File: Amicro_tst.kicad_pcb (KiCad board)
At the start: 2 copper layers, 16 parts, among them J1 Conn_01x04_Female, J2 Conn_01x05_Female, J3 Conn_01x04_Female, SW1 SW_Push, U1 ATmega328-P, U2 24LC512, Y1 Crystal

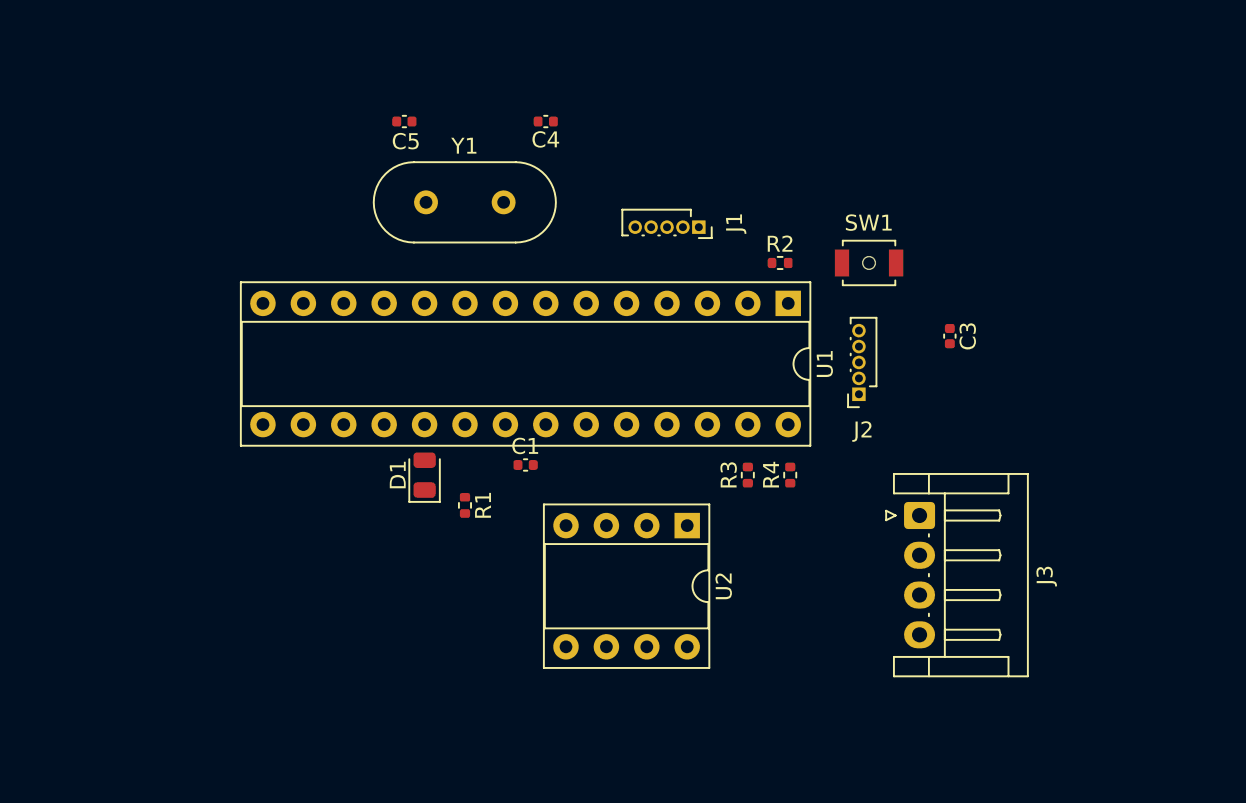
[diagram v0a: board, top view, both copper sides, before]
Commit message: redid lost work/testpoints
Redid lost work that didnt save, still need to find footprints for transistors
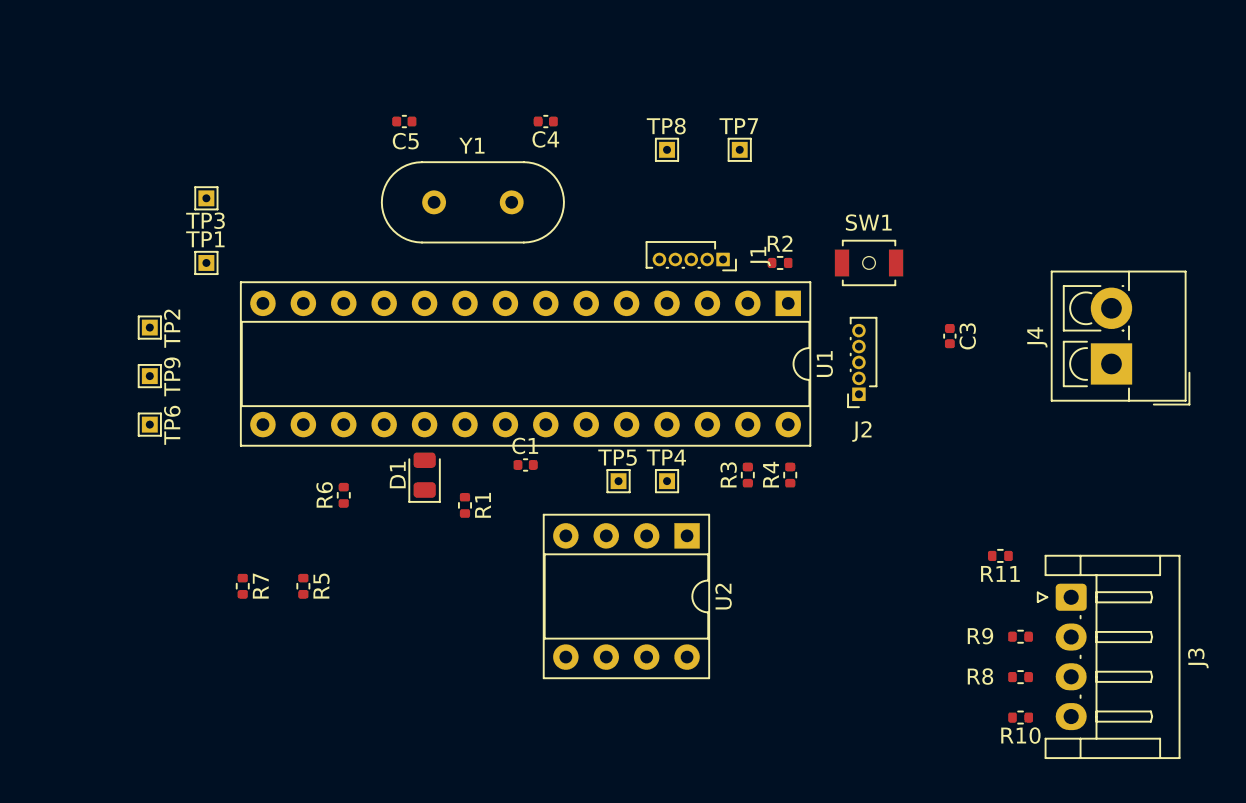
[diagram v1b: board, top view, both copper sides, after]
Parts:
- added J4: Screw_Terminal_01x02, TerminalBlock_4Ucon:TerminalBlock_4Ucon_1x02_P3.50mm_Vertical, F.Cu at (166.0, 124.1)
- added R10: 33, Resistor_SMD:R_0402_1005Metric, F.Cu at (160.3, 146.4)
- added R11: 33, Resistor_SMD:R_0402_1005Metric, F.Cu at (159.1, 136.2)
- added R5: 1k, Resistor_SMD:R_0402_1005Metric, F.Cu at (115.2, 138.1)
- added R6: 1k, Resistor_SMD:R_0402_1005Metric, F.Cu at (117.8, 132.4)
- added R7: 1k, Resistor_SMD:R_0402_1005Metric, F.Cu at (111.4, 138.1)
- added R8: 33, Resistor_SMD:R_0402_1005Metric, F.Cu at (160.3, 143.8)
- added R9: 33, Resistor_SMD:R_0402_1005Metric, F.Cu at (160.3, 141.3)
- added TP1: TstPin, TestPoint:TestPoint_THTPad_1.0x1.0mm_Drill0.5mm, F.Cu at (109.1, 117.8)
- added TP2: TstPin, TestPoint:TestPoint_THTPad_1.0x1.0mm_Drill0.5mm, F.Cu at (105.6, 121.8)
- added TP3: TstPin, TestPoint:TestPoint_THTPad_1.0x1.0mm_Drill0.5mm, F.Cu at (109.1, 113.7)
- added TP4: TstPin, TestPoint:TestPoint_THTPad_1.0x1.0mm_Drill0.5mm, F.Cu at (138.1, 131.5)
- added TP5: TstPin, TestPoint:TestPoint_THTPad_1.0x1.0mm_Drill0.5mm, F.Cu at (135.1, 131.5)
- added TP6: TstPin, TestPoint:TestPoint_THTPad_1.0x1.0mm_Drill0.5mm, F.Cu at (105.6, 127.9)
- added TP7: TstPin, TestPoint:TestPoint_THTPad_1.0x1.0mm_Drill0.5mm, F.Cu at (142.7, 110.7)
- added TP8: TstPin, TestPoint:TestPoint_THTPad_1.0x1.0mm_Drill0.5mm, F.Cu at (138.1, 110.7)
- added TP9: TstPin, TestPoint:TestPoint_THTPad_1.0x1.0mm_Drill0.5mm, F.Cu at (105.6, 124.9)
- moved J3 10.8 mm to (163.5, 138.8)
- moved J1 2.54 mm to (141.6, 117.6)
- moved U2 0.65 mm to (139.4, 134.9)
- moved Y1 0.51 mm to (123.5, 114.0)
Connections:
- J3 pad 1: unconnected-(J3-Pad1) -> Net-(J3-Pad1)
- J3 pad 2: unconnected-(J3-Pad2) -> Net-(J3-Pad2)
- J3 pad 3: unconnected-(J3-Pad3) -> Net-(J3-Pad3)
- J3 pad 4: unconnected-(J3-Pad4) -> Net-(J3-Pad4)
- U1 pad 12: unconnected-(U1-Pad12) -> Net-(U1-Pad12)
- U1 pad 13: unconnected-(U1-Pad13) -> Net-(U1-Pad13)
- U1 pad 14: unconnected-(U1-Pad14) -> Net-(U1-Pad14)
- U1 pad 15: unconnected-(U1-Pad15) -> PWM0
- U1 pad 16: unconnected-(U1-Pad16) -> PWM1
- U1 pad 17: unconnected-(U1-Pad17) -> PWM2
- U1 pad 24: unconnected-(U1-Pad24) -> Net-(U1-Pad24)
- U1 pad 25: unconnected-(U1-Pad25) -> Net-(U1-Pad25)
- U1 pad 26: unconnected-(U1-Pad26) -> Net-(U1-Pad26)
- U1 pad 4: unconnected-(U1-Pad4) -> Net-(U1-Pad4)
- U1 pad 5: unconnected-(U1-Pad5) -> Net-(U1-Pad5)
- U1 pad 6: unconnected-(U1-Pad6) -> Net-(U1-Pad6)

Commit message: transistor footprints
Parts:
- added Q1: Q_NPN_BEC, TO_SOT_Packages_SMD:SC-59_Handsoldering, F.Cu at (124.4, 136.6)
- added Q2: Q_NPN_BEC, TO_SOT_Packages_SMD:SC-59_Handsoldering, F.Cu at (119.3, 136.1)
- added Q3: Q_NPN_BEC, TO_SOT_Packages_SMD:SC-59_Handsoldering, F.Cu at (114.7, 136.1)
- J1: footprint Connector_PinSocket_1.00mm:PinSocket_1x05_P1.00mm_Vertical -> Connector_JST:JST_EH_S4B-EH_1x04_P2.50mm_Horizontal
- moved J3 56.9 mm to (107.1, 145.9), turned to 90 degrees
- moved R10 50.7 mm to (110.3, 138.4), turned to 0 degrees
- moved R8 50.1 mm to (110.3, 140.9), turned to 180 degrees
- moved R9 50.1 mm to (110.3, 143.4), turned to 0 degrees
- moved R11 45.2 mm to (115.7, 149.3), turned to 0 degrees
- moved R3 18.8 mm to (132.0, 146.2), turned to -90 degrees
- moved R4 18.3 mm to (135.6, 146.2), turned to -90 degrees
- moved TP3 9.16 mm to (118.3, 114.2)
- moved J1 8.79 mm to (148.6, 112.2), turned to 0 degrees
- moved R7 7.62 mm to (111.7, 130.5)
- moved R5 7.62 mm to (115.2, 130.5)
- moved TP1 7.06 mm to (115.2, 114.2)
- moved TP5 3.05 mm to (138.1, 131.5)
- moved TP4 2.54 mm to (135.6, 131.5)
- moved R6 2.16 mm to (118.8, 130.5)
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
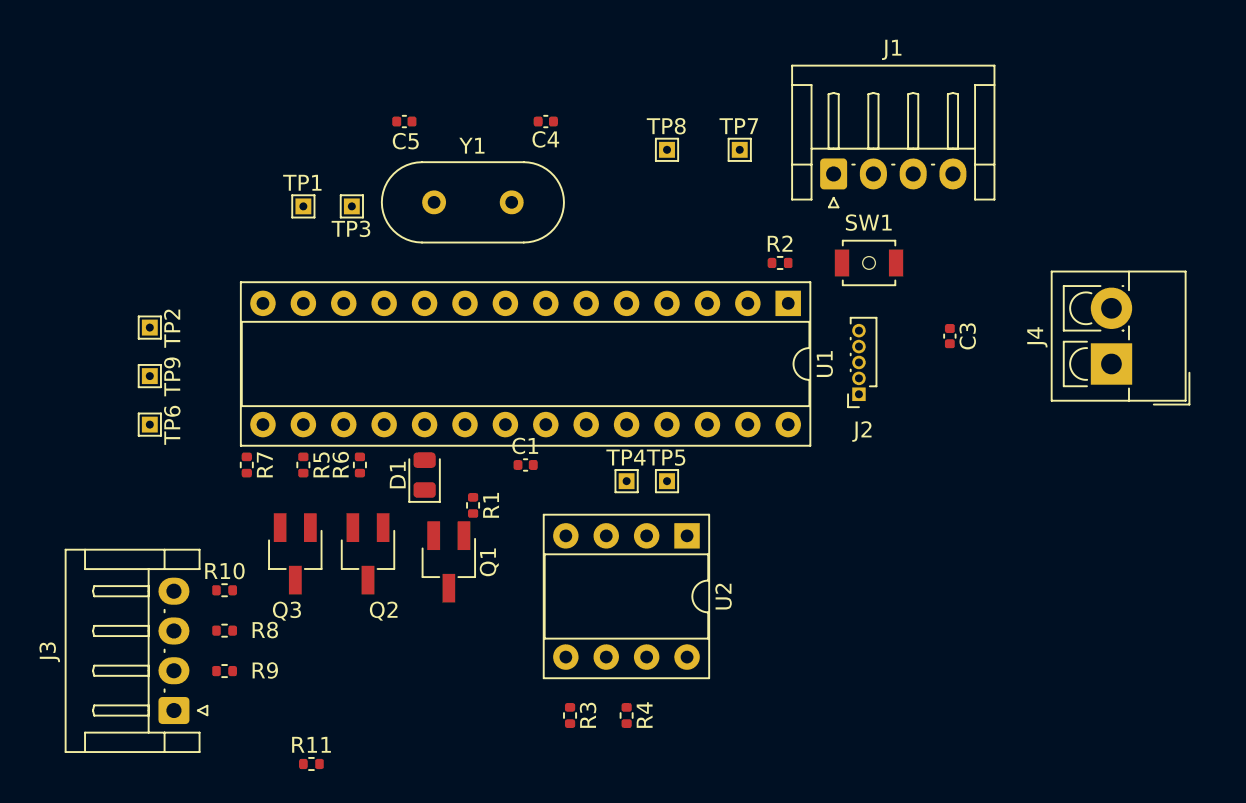
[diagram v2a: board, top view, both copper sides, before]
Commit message: Changed Footprints & Board Size
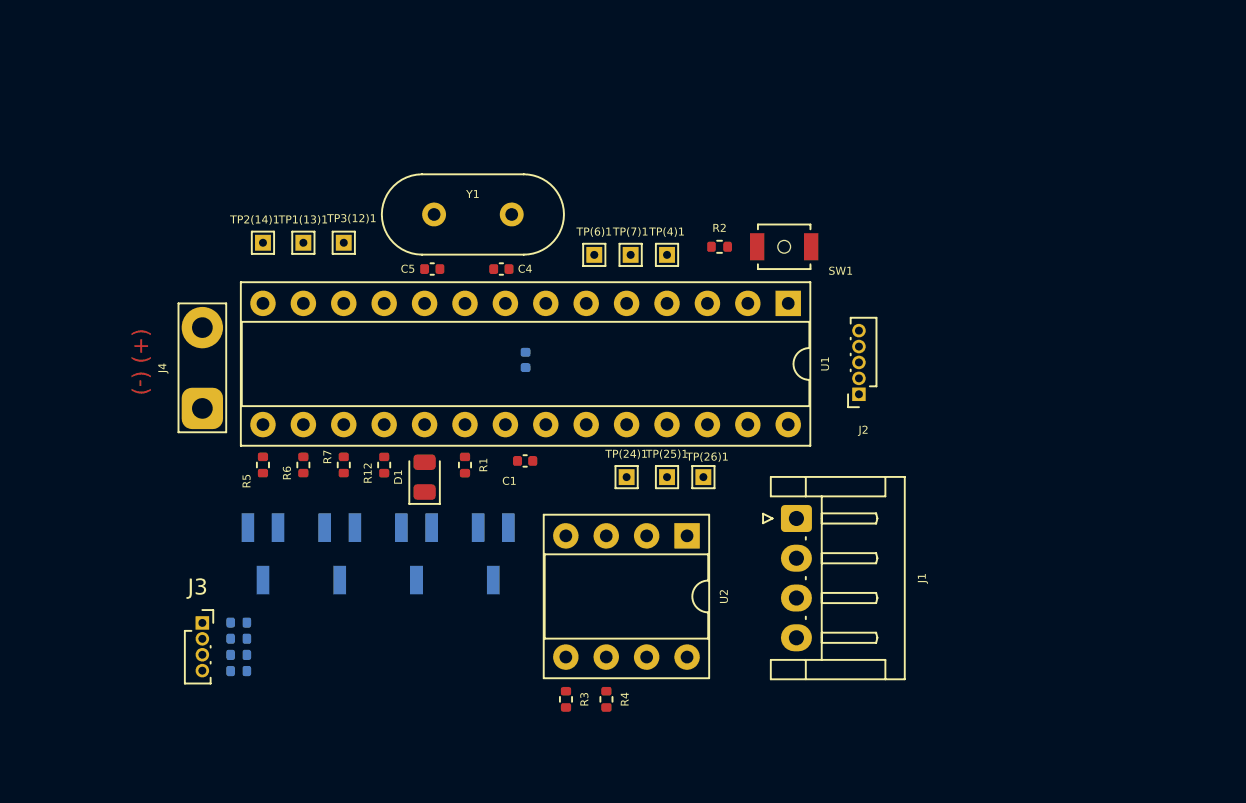
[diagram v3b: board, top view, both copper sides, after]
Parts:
- added Q4: Q_NPN_BEC, Package_TO_SOT_SMD:SC-59_Handsoldering, B.Cu at (127.2, 136.1)
- added R12: 1k, Resistor_SMD:R_0402_1005Metric, F.Cu at (120.3, 130.5)
- C3, R10, R11, R8, R9: moved to B.Cu
- J1: value Conn_01x04_Female -> Sensor
- J3: value Conn_01x04_Female -> Vibr; footprint Connector_JST:JST_EH_S4B-EH_1x04_P2.50mm_Horizontal -> Connector_PinSocket_1.00mm:PinSocket_1x04_P1.00mm_Vertical
- J4: value Screw_Terminal_01x02 -> Pow; footprint TerminalBlock_4Ucon:TerminalBlock_4Ucon_1x02_P3.50mm_Vertical -> TestPoint:TestPoint_2Pads_Pitch5.08mm_Drill1.3mm
- Q1: renamed from Q3; footprint TO_SOT_Packages_SMD:SC-59_Handsoldering -> Package_TO_SOT_SMD:SC-59_Handsoldering; moved to B.Cu
- Q2: renamed from Q1; footprint TO_SOT_Packages_SMD:SC-59_Handsoldering -> Package_TO_SOT_SMD:SC-59_Handsoldering; moved to B.Cu
- Q3: renamed from Q2; footprint TO_SOT_Packages_SMD:SC-59_Handsoldering -> Package_TO_SOT_SMD:SC-59_Handsoldering; moved to B.Cu
- SW1: value SW_Push -> RESET
- TP(24)1: renamed from TP4; value TstPin -> TP
- TP(25)1: renamed from TP5; value TstPin -> TP
- TP(26)1: renamed from TP6; value TstPin -> TP
- TP(4)1: renamed from TP7; value TstPin -> TP
- TP(6)1: renamed from TP9; value TstPin -> TP
- TP(7)1: renamed from TP8; value TstPin -> TP
- TP1(13)1: renamed from TP1; value TstPin -> TP
- TP2(14)1: renamed from TP2; value TstPin -> TP
- TP3(12)1: renamed from TP3; value TstPin -> TP
- moved J4 57.2 mm to (108.9, 126.9)
- moved TP(26)1 35.0 mm to (140.4, 131.2), turned to 0 degrees
- moved TP(6)1 29.0 mm to (133.5, 117.3), turned to 0 degrees
- moved C3 26.7 mm to (129.2, 123.9)
- moved J1 21.8 mm to (146.2, 133.8), turned to -90 degrees
- moved C4 9.68 mm to (127.7, 118.2), turned to 0 degrees
- moved C5 9.43 mm to (123.3, 118.2)
- moved R11 9.11 mm to (111.2, 141.4), turned to 180 degrees
- moved TP2(14)1 8.89 mm to (112.7, 116.5), turned to 0 degrees
- moved TP(4)1 8.03 mm to (138.1, 117.3)
- moved TP(7)1 6.99 mm to (135.8, 117.3)
- moved Q2 6.88 mm to (117.5, 136.1)
- moved J3 5.79 mm to (108.9, 140.4), turned to 0 degrees
- moved SW1 5.43 mm to (145.5, 116.8)
- moved R2 3.94 mm to (141.4, 116.8)
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- renumbered R7 to R5, R5 to R6, R6 to R7
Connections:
- J1 pad 4: /5V -> VCC
- J3 pad 1: Net-(J3-Pad1) -> Net-(R10-Pad2)
- J3 pad 2: Net-(J3-Pad2) -> Net-(R11-Pad2)
- J3 pad 3: Net-(J3-Pad3) -> Net-(R9-Pad2)
- J3 pad 4: Net-(J3-Pad4) -> Net-(R8-Pad2)
- Q1 pad 3: Net-(Q3-Pad3) -> Net-(Q1-Pad3)
- Q2 pad 3: Net-(Q1-Pad3) -> Net-(R11-Pad1)
- Q3 pad 3: Net-(Q2-Pad3) -> Net-(Q3-Pad3)
- R10 pad 1: unconnected-(R10-Pad1) -> Net-(Q1-Pad3)
- R10 pad 2: Net-(J3-Pad4) -> Net-(R10-Pad2)
- R11 pad 1: Net-(Q3-Pad3) -> Net-(R11-Pad1)
- R11 pad 2: Net-(J3-Pad1) -> Net-(R11-Pad2)
- R8 pad 1: Net-(Q2-Pad3) -> Net-(R8-Pad1)
- R8 pad 2: Net-(J3-Pad3) -> Net-(R8-Pad2)
- R9 pad 1: Net-(Q1-Pad3) -> Net-(Q3-Pad3)
- R9 pad 2: Net-(J3-Pad2) -> Net-(R9-Pad2)
- U1 pad 18: unconnected-(U1-Pad18) -> PWM3
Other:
- board text added: "(+) (-)"
